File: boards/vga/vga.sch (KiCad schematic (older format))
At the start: 26 parts

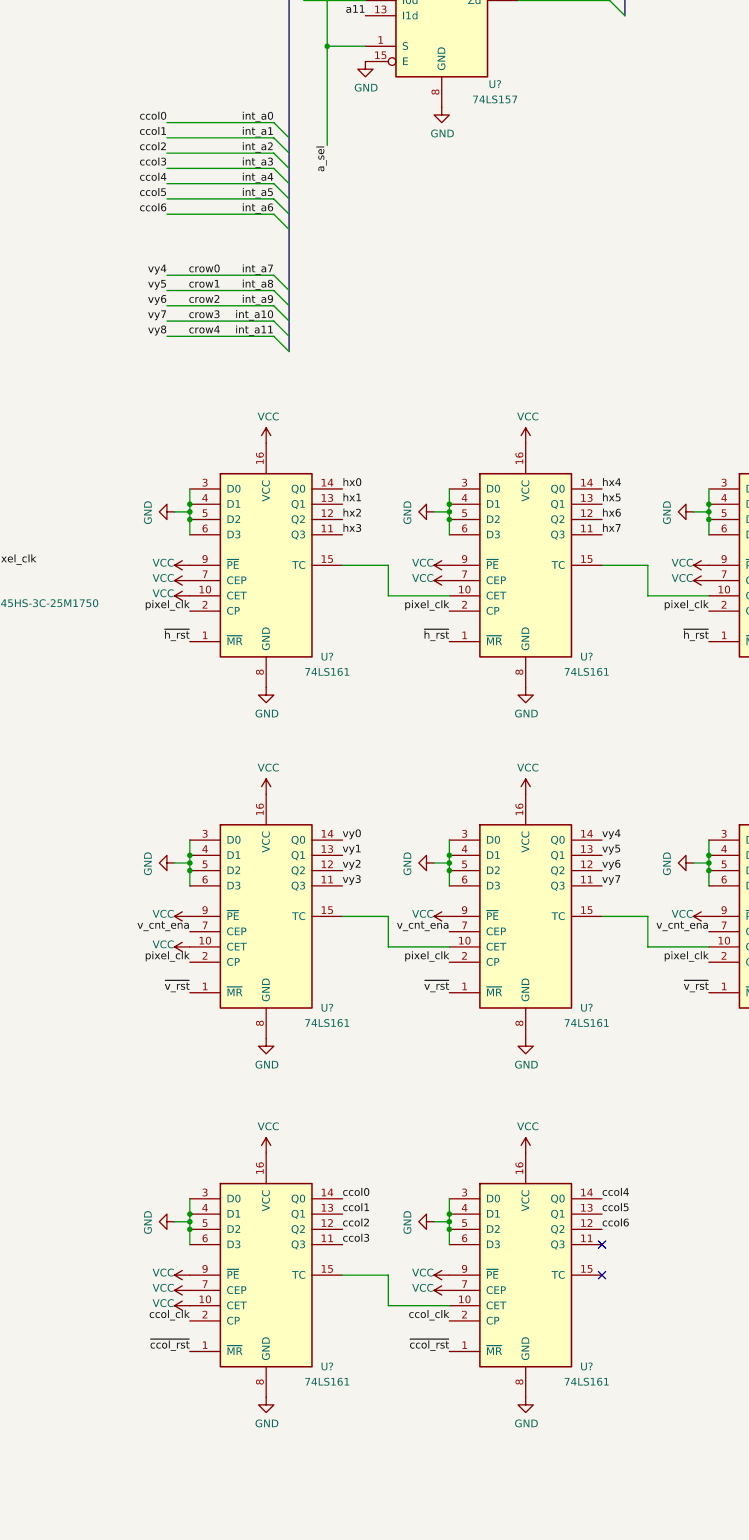
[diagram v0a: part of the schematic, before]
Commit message: Remove ccol counter
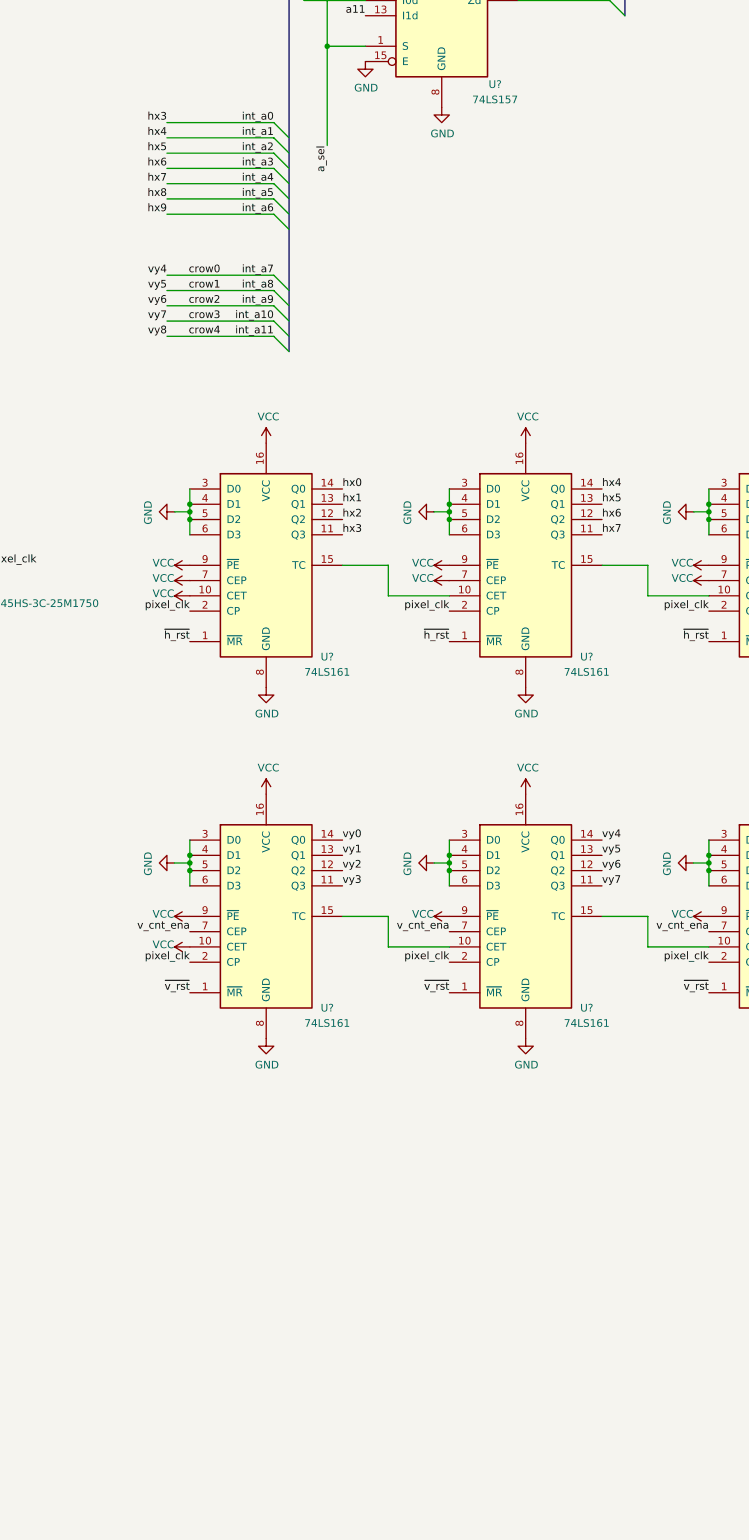
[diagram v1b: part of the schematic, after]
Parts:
- removed U? (x2): 74LS161, symbol 74xx:74LS161
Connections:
- net ccol0 is gone; now on net hx3: U?.2 (I0a)
- net ccol1 is gone; now on net hx4: U?.5 (I0b)
- net ccol2 is gone; now on net hx5: U?.11 (I0c)
- net ccol3 is gone; now on net hx6: U?.14 (I0d)
- net ccol4 is gone; now on net hx7: U?.2 (I0a)
- net ccol5 is gone; now on net hx8: U?.5 (I0b)
- net ccol6 is gone; now on net hx9: U?.11 (I0c)
- no-connect marks 17 -> 15
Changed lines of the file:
@@
 vy8
 Text Label 3050 10950 2    50   ~ 0
-ccol0
+hx3
 Text Label 3050 11050 2    50   ~ 0
-ccol1
+hx4
 Text Label 3050 11150 2    50   ~ 0
-ccol2
+hx5
 Text Label 3050 11250 2    50   ~ 0
-ccol3
+hx6
 Text Label 3050 11350 2    50   ~ 0
-ccol4
+hx7
 Text Label 3050 11450 2    50   ~ 0
-ccol5
+hx8
 Text Label 3050 11550 2    50   ~ 0
-ccol6
+hx9
 $Comp
 L power:GND #PWR?
@@
 NoConn ~ 7600 15850
 NoConn ~ 7600 15950
-$Comp
-L 74xx:74LS161 U?
-U 1 1 6012E395
-P 3700 18500
-F 0 "U?" H 4100 17900 50  0000 C CNN
-F 1 "74LS161" H 4100 17800 50  0000 C CNN
-F 2 "" H 3700 18500 50  0001 C CNN
-F 3 "http://www.ti.com/lit/gpn/sn74LS161" H 3700 18500 50  0001 C CNN
-	1    3700 18500
-	1    0    0    -1
-$EndComp
-$Comp
-L power:GND #PWR?
-U 1 1 6012E39B
-P 3700 19300
-F 0 "#PWR?" H 3700 19050 50  0001 C CNN
-F 1 "GND" H 3705 19127 50  0000 C CNN
-F 2 "" H 3700 19300 50  0001 C CNN
-F 3 "" H 3700 19300 50  0001 C CNN
-	1    3700 19300
-	1    0    0    -1
-$EndComp
-$Comp
-L power:VCC #PWR?
-U 1 1 6012E3A1
-P 3700 17700
-F 0 "#PWR?" H 3700 17550 50  0001 C CNN
-F 1 "VCC" H 3715 17873 50  0000 C CNN
-F 2 "" H 3700 17700 50  0001 C CNN
-F 3 "" H 3700 17700 50  0001 C CNN
-	1    3700 17700
-	1    0    0    -1
-$EndComp
-$Comp
-L power:GND #PWR?
-U 1 1 6012E3A7
-P 3100 18150
-F 0 "#PWR?" H 3100 17900 50  0001 C CNN
-F 1 "GND" H 3105 17977 50  0000 C CNN
-F 2 "" H 3100 18150 50  0001 C CNN
-F 3 "" H 3100 18150 50  0001 C CNN
-	1    3100 18150
-	0    1    1    0
-$EndComp
-Wire Wire Line
-	3200 18000 3200 18100
-Connection ~ 3200 18100
-Wire Wire Line
-	3200 18100 3200 18150
-Connection ~ 3200 18200
-Wire Wire Line
-	3200 18200 3200 18300
-Wire Wire Line
-	3100 18150 3200 18150
-Connection ~ 3200 18150
-Wire Wire Line
-	3200 18150 3200 18200
-$Comp
-L power:VCC #PWR?
-U 1 1 6012E3B5
-P 3200 18500
-F 0 "#PWR?" H 3200 18350 50  0001 C CNN
-F 1 "VCC" V 3215 18673 50  0000 C CNN
-F 2 "" H 3200 18500 50  0001 C CNN
-F 3 "" H 3200 18500 50  0001 C CNN
-	1    3200 18500
-	0    -1   -1   0
-$EndComp
-$Comp
-L power:VCC #PWR?
-U 1 1 6012E3BB
-P 3200 18600
-F 0 "#PWR?" H 3200 18450 50  0001 C CNN
-F 1 "VCC" V 3215 18773 50  0000 C CNN
-F 2 "" H 3200 18600 50  0001 C CNN
-F 3 "" H 3200 18600 50  0001 C CNN
-	1    3200 18600
-	0    -1   -1   0
-$EndComp
-$Comp
-L 74xx:74LS161 U?
-U 1 1 6012E3C1
-P 5400 18500
-F 0 "U?" H 5800 17900 50  0000 C CNN
-F 1 "74LS161" H 5800 17800 50  0000 C CNN
-F 2 "" H 5400 18500 50  0001 C CNN
-F 3 "http://www.ti.com/lit/gpn/sn74LS161" H 5400 18500 50  0001 C CNN
-	1    5400 18500
-	1    0    0    -1
-$EndComp
-$Comp
-L power:GND #PWR?
-U 1 1 6012E3C7
-P 5400 19300
-F 0 "#PWR?" H 5400 19050 50  0001 C CNN
-F 1 "GND" H 5405 19127 50  0000 C CNN
-F 2 "" H 5400 19300 50  0001 C CNN
-F 3 "" H 5400 19300 50  0001 C CNN
-	1    5400 19300
-	1    0    0    -1
-$EndComp
-$Comp
-L power:VCC #PWR?
-U 1 1 6012E3CD
-P 5400 17700
-F 0 "#PWR?" H 5400 17550 50  0001 C CNN
-F 1 "VCC" H 5415 17873 50  0000 C CNN
-F 2 "" H 5400 17700 50  0001 C CNN
-F 3 "" H 5400 17700 50  0001 C CNN
-	1    5400 17700
-	1    0    0    -1
-$EndComp
-$Comp
-L power:GND #PWR?
-U 1 1 6012E3D3
-P 4800 18150
-F 0 "#PWR?" H 4800 17900 50  0001 C CNN
-F 1 "GND" H 4805 17977 50  0000 C CNN
-F 2 "" H 4800 18150 50  0001 C CNN
-F 3 "" H 4800 18150 50  0001 C CNN
-	1    4800 18150
-	0    1    1    0
-$EndComp
-Wire Wire Line
-	4900 18000 4900 18100
-Connection ~ 4900 18100
-Wire Wire Line
-	4900 18100 4900 18150
-Connection ~ 4900 18200
-Wire Wire Line
-	4900 18200 4900 18300
-Wire Wire Line
-	4800 18150 4900 18150
-Connection ~ 4900 18150
-Wire Wire Line
-	4900 18150 4900 18200
-$Comp
-L power:VCC #PWR?
-U 1 1 6012E3E1
-P 4900 18500
-F 0 "#PWR?" H 4900 18350 50  0001 C CNN
-F 1 "VCC" V 4915 18673 50  0000 C CNN
-F 2 "" H 4900 18500 50  0001 C CNN
-F 3 "" H 4900 18500 50  0001 C CNN
-	1    4900 18500
-	0    -1   -1   0
-$EndComp
-$Comp
-L power:VCC #PWR?
-U 1 1 6012E3E7
-P 4900 18600
-F 0 "#PWR?" H 4900 18450 50  0001 C CNN
-F 1 "VCC" V 4915 18773 50  0000 C CNN
-F 2 "" H 4900 18600 50  0001 C CNN
-F 3 "" H 4900 18600 50  0001 C CNN
-	1    4900 18600
-	0    -1   -1   0
-$EndComp
-Wire Wire Line
-	4200 18500 4500 18500
-Wire Wire Line
-	4500 18500 4500 18700
-Wire Wire Line
-	4500 18700 4900 18700
-$Comp
-L power:VCC #PWR?
-U 1 1 6012E420
-P 3200 18700
-F 0 "#PWR?" H 3200 18550 50  0001 C CNN
-F 1 "VCC" V 3215 18873 50  0000 C CNN
-F 2 "" H 3200 18700 50  0001 C CNN
-F 3 "" H 3200 18700 50  0001 C CNN
-	1    3200 18700
-	0    -1   -1   0
-$EndComp
-Text Label 3200 18800 2    50   ~ 0
-ccol_clk
-Text Label 4900 18800 2    50   ~ 0
-ccol_clk
-Text Label 3200 19000 2    50   ~ 0
-~ccol_rst
-Text Label 4900 19000 2    50   ~ 0
-~ccol_rst
 Text Label 4200 15650 0    50   ~ 0
 vy0
@@
 Text Label 6600 16650 2    50   ~ 0
 ~v_rst
-NoConn ~ 5900 18500
-Text Label 4200 18000 0    50   ~ 0
-ccol0
-Text Label 4200 18100 0    50   ~ 0
-ccol1
-Text Label 4200 18200 0    50   ~ 0
-ccol2
-Text Label 4200 18300 0    50   ~ 0
-ccol3
-Text Label 5900 18000 0    50   ~ 0
-ccol4
-Text Label 5900 18100 0    50   ~ 0
-ccol5
-Text Label 5900 18200 0    50   ~ 0
-ccol6
-NoConn ~ 5900 18300
 $Comp
 L Oscillator:CXO_DIP8 X?

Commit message: Buffered hsync, some of the VGA schematic
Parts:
- added U14: 74LS20, symbol 74xx:74LS20
- added U15, U25: 74LS32, symbol 74xx:74LS32
- added U16: 74LS08, symbol 74xx:74LS08
- added U22: 74LS10, symbol 74xx:74LS10
- added U23: 74LS74, symbol 74xx:74LS74
- added U24: 74LS00, symbol 74xx:74LS00
- added U26: 74LS21, symbol 74xx:74LS21
- gave numbers to parts that had none: 24
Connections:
- net VCC: now also U23.1 (~R), U23.13 (~R)
- net crow0: now also U25.1
- net crow1: now also U26.5
- net crow2: now also U26.4
- net crow3: now also U26.2
- net crow4: now also U26.1
- net hx4: now also U15.5, U22.13
- net hx5: now also U15.2, U22.2
- net hx6: now also U15.1, U22.1
- net hx7: now also U14.4, U15.10
- net hx8: now also U15.9
- net hx9: now also U14.2, U24.2
- net vy0: now also U14.13
- net vy1: now also U22.5
- net vy2: now also U14.12, U25.2
- net vy3: now also U14.10, U22.4
- net vy9: now also U14.9, U24.9
- net ~pixel_ena: now also U23.9 (Q)
- net ~rst: now also U16.10, U23.10 (~S), U23.4 (~S)
- net ~v_rst: now also U16.8
- new net: U14.6, U23.2 (D)
- new net: U25.3, U25.4
- new net hsync_out: U23.5 (Q)
- new net hx_6_0_lt_1110000: U14.1, U22.12
- new net hx_lt_640: U24.3, U24.4
- new net hx_or_65: U15.3, U15.4
- new net hx_or_654: U14.5, U15.6
- new net hx_or_87: U15.8, U24.1
- new net pixel_ena: U23.8 (~Q)
- new net vsync_out: U25.6
- new net vy_8765: U22.3, U24.10, U26.6
- new net vy_lt_480: U24.5, U24.8
- new net vy_nand_3: U22.6, U25.5
- new net vy_nand_9320: U14.8, U16.9
- new net ~hsync_out: U23.6 (~Q)
- new net ~hx2: U23.11 (C), U23.3 (C)
- new net ~pixel_ena_int: U23.12 (D), U24.6

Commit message: 74LV-A chips and their delays
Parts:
- added R1: 50, symbol Device:R
- added U27: SN74LV86APWR, Package_SO:TSSOP-14_4.4x5mm_P0.65mm, symbol 74xx:74LS86
- added U? (x3): SN74LV20APWR, Package_SO:TSSOP-14_4.4x5mm_P0.65mm, symbol 74xx:74LS20
- U14: value 74LS20 -> SN74LV20APWR; footprint (none) -> Package_SO:TSSOP-14_4.4x5mm_P0.65mm
- U15, U25: value 74LS32 -> 74LV32APWJ; footprint (none) -> Package_SO:TSSOP-14_4.4x5mm_P0.65mm
- U16: value 74LS08 -> 74LV08APWJ; footprint (none) -> Package_SO:TSSOP-14_4.4x5mm_P0.65mm
- U22: value 74LS10 -> SN74LV10APWR; footprint (none) -> Package_SO:TSSOP-14_4.4x5mm_P0.65mm
- U24: value 74LS00 -> SN74LV00APW; footprint (none) -> Package_SO:TSSOP-14_4.4x5mm_P0.65mm
- U26: value 74LS21 -> SN74LV21APWR; footprint (none) -> Package_SO:TSSOP-14_4.4x5mm_P0.65mm
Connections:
- net v_cnt_ena is gone; now on net VCC: U12.7 (CEP), U2.7 (CEP), U7.7 (CEP)
- net ~pixel_ena_int is gone; now on net a_sel: U23.12 (D), U24.6
- net VCC: now also U27.2
- net a12: now also U27.5
- net a13: now also U27.4
- net a14: now also U?.4
- net a15: now also U?.2
- net a_sel: now also U27.1
- net ena: now also U?.5
- net hx5: now also U22.11
- net hx8: now also U22.10
- net hx9: now also U22.9
- net pixel_clk: no longer U12.2 (CP), U2.2 (CP), U7.2 (CP)
- net ~h_rst: now also U16.11
- net ~hsync_out: now also R1.1
- net ~rst: now also U16.13
- net at U16.12: now also U22.8
- new net a_13_xor_12: U27.6, U?.1
- new net ram_busy: U27.3
- new net v_clk: R1.2, U12.2 (CP), U2.2 (CP), U7.2 (CP)
- new net ~ext_sel: U?.6
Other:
- moved on the sheet: U16A, U16D, U22C

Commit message: VGA control logic on schematic
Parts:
- removed U27: SN74LV86APWR, Package_SO:TSSOP-14_4.4x5mm_P0.65mm, symbol 74xx:74LS86
- removed U? (x3): SN74LV20APWR, Package_SO:TSSOP-14_4.4x5mm_P0.65mm, symbol 74xx:74LS20
- added Q1: Q_PMOS_DGS, symbol Device:Q_PMOS_DGS
- added R?: 50, symbol Device:R
- added U27: SN74AHC1G86DBVR, Package_TO_SOT_SMD:SOT-23-5, symbol 74xGxx:74LVC1G86
- added U28: 74LV32APWJ, Package_SO:TSSOP-14_4.4x5mm_P0.65mm, symbol 74xx:74LS32
- added U29: 74LV08APWJ, Package_SO:TSSOP-14_4.4x5mm_P0.65mm, symbol 74xx:74LS08
- added U30: SN74LV74APWR, Package_SO:TSSOP-14_4.4x5mm_P0.65mm, symbol 74xx:74LS74
- U23: value 74LS74 -> SN74LV74APWR; footprint (none) -> Package_SO:TSSOP-14_4.4x5mm_P0.65mm
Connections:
- net ~color_ram_oe is gone; now on net a_sel: U10.1 (~OE)
- net ~d_to_color_oe is gone; now on net ~color_ram_we: U13.1 (1OE), U13.19 (2OE)
- net ~text_ram_oe is gone; now on net a_sel: U9.1 (~OE)
- net ~text_ram_we is gone; now on net ~d_to_text_oe: U9.6 (~WE)
- net GND: now also U14.7 (GND), U15.7 (GND), U16.7 (GND), U22.7 (GND), U23.7 (GND), U24.7 (GND), U25.7 (GND), U26.7 (GND), U27.3 (GND), U28.7 (GND), U29.7 (GND), U30.7 (GND)
- net VCC: now also U14.14 (VCC), U15.14 (VCC), U16.1, U16.14 (VCC), U16.2, U22.14 (VCC), U23.14 (VCC), U24.14 (VCC), U25.14 (VCC), U26.14 (VCC), Q1.3 (S), U27.5 (VCC), U28.10, U28.14 (VCC), U28.9, U29.14 (VCC), U30.1 (~R), U30.10 (~S), U30.11 (C), U30.12 (D), U30.13 (~R), U30.14 (VCC)
- net a12: now also U24.5, U25.12, U27.2
- net a13: now also U27.1
- net a14: now also U26.12
- net a15: now also U26.10
- net a_13_xor_12: now also U26.9, U27.4
- net a_sel: now also U28.11, U29.10, U29.13; no longer U23.12 (D), U24.6
- net ena: now also U26.13
- net hx0: now also R?.1
- net hx2: now also U24.12, U24.13
- net hx9: now also U16.5; no longer U24.2
- net hx_or_87: now also U16.4; no longer U24.1
- net vy9: now also U28.1; no longer U24.9
- net vy_8765: now also U28.2; no longer U24.10
- net ~color_ram_cs: now also U29.8
- net ~color_ram_we: now also U15.11, U24.2, U29.9
- net ~d_to_text_oe: now also U24.1, U25.8, U29.12
- net ~hx2: now also U24.11
- net ~rdy: now also Q1.1 (D)
- net ~rst: now also U30.4 (~S)
- net ~text_ram_cs: now also U29.11
- net ~we: now also U15.13, U25.13
- net hsync_int: now reaches U14.6, U23.2 (D)
- net at U15.12: now also U24.6
- net ~hx_lt_640: now reaches U16.6
- net ~hx_lt_640: now also U28.5
- net or_a12_nwe: now reaches U25.10
- net or_a12_nwe: now also U25.11
- net ~acc_req: now reaches U25.9
- net ~acc_req: now also U24.8
- net ext_sel: now reaches U26.8
- net ext_sel: now also U29.5
- net hx_lt_640 renamed acc_req
- net acc_req: now also U24.10, U24.9, U29.6; no longer U24.3
- removed net vy_lt_480: U24.5, U24.8
- new net a_sel_clk: R?.2, U30.3 (C)
- new net buf_a_sel: U28.12, U29.2, U30.5 (Q)
- new net ext_acc_ena: U29.3, U29.4
- new net rdy_out: Q1.2 (G), U24.3
- new net ~pixel_ena_int: U23.12 (D), U28.13, U28.6, U29.1, U30.2 (D)
- new net ~vy_lt_480: U28.3, U28.4
- no-connect marks 15 -> 20
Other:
- note added: "see /model/vga_ctrl.v"
- moved on the sheet: U14C, U15D, U15E, U16A, U16B, U16E, U22D, U23C, U24A, U24B, U24C, U24D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

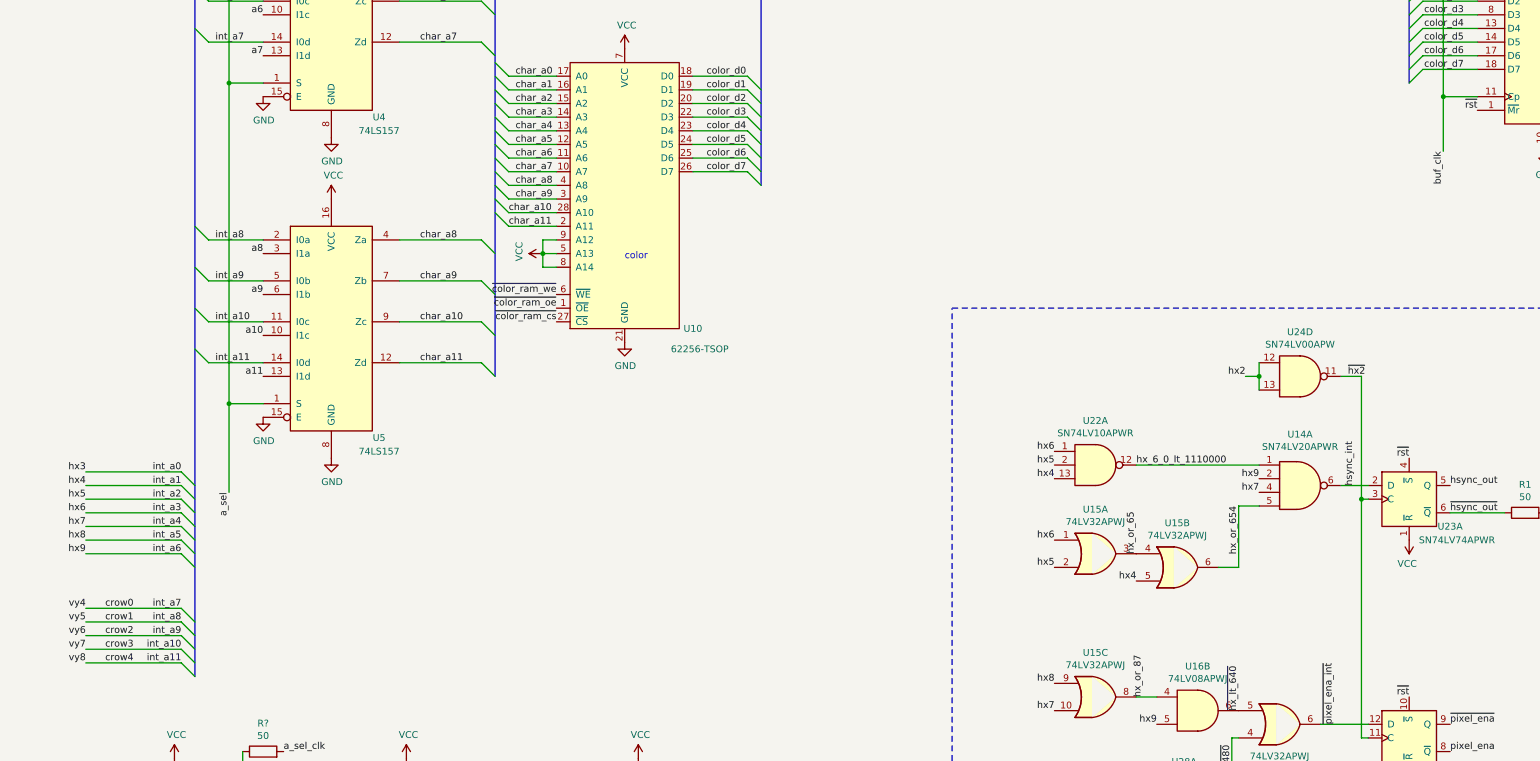
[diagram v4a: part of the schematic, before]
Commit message: Check overall VGA schematic
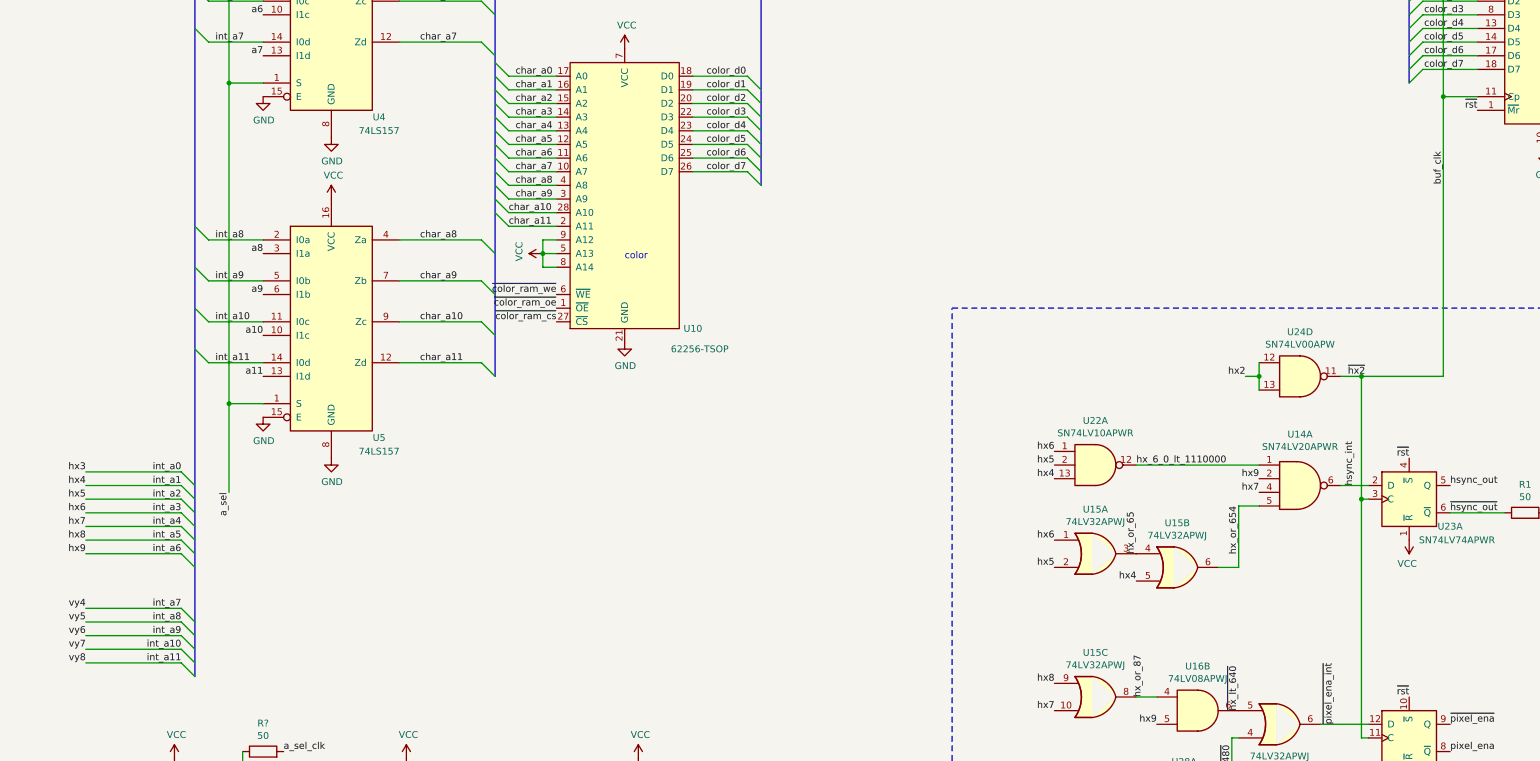
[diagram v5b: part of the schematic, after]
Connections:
- net ~hx2 is gone; now on net buf_clk: U23.11 (C), U23.3 (C), U24.11
- net crow0 renamed int_a7
- net crow1 renamed int_a8
- net crow2 renamed int_a9
- net crow3 renamed int_a10
- net crow4 renamed int_a11
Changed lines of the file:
@@
 Text Label 3750 12350 2    50   ~ 0
 int_a11
-Text Label 3400 11950 2    50   ~ 0
-crow0
-Text Label 3400 12050 2    50   ~ 0
-crow1
-Text Label 3400 12150 2    50   ~ 0
-crow2
-Text Label 3400 12250 2    50   ~ 0
-crow3
-Text Label 3400 12350 2    50   ~ 0
-crow4
 Text Label 3050 11950 2    50   ~ 0
 vy4
@@
 Wire Wire Line
 	13000 8200 13250 8200
-Wire Wire Line
-	13000 8200 13000 8600
 Connection ~ 13000 8200
 Text Label 13000 8600 3    50   ~ 0
@@
 Wire Notes Line
 	22550 17150 9400 17150
+Text Notes 17650 10350 0    197  ~ 0
+see /model/vga_ctrl.v
+Wire Wire Line
+	12400 10250 13000 10250
+Wire Wire Line
+	13000 8200 13000 10250
 Wire Bus Line
 	11050 5150 11050 5850
@@
 Wire Bus Line
 	6050 4500 6050 10250
-Text Notes 17650 10350 0    197  ~ 0
-see /model/vga_ctrl.v
+Connection ~ 12400 10250
 $EndSCHEMATC
